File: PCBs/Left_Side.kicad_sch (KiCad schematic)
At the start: 77 parts, among them J1 USB_C_Receptacle, J3 USB_C_Receptacle, U1 W25Q128JVS, U2 XC6206-3.3_SOT, U3 USBLC6-2SC6, U4 RP2040, Y1 Crystal_GND24

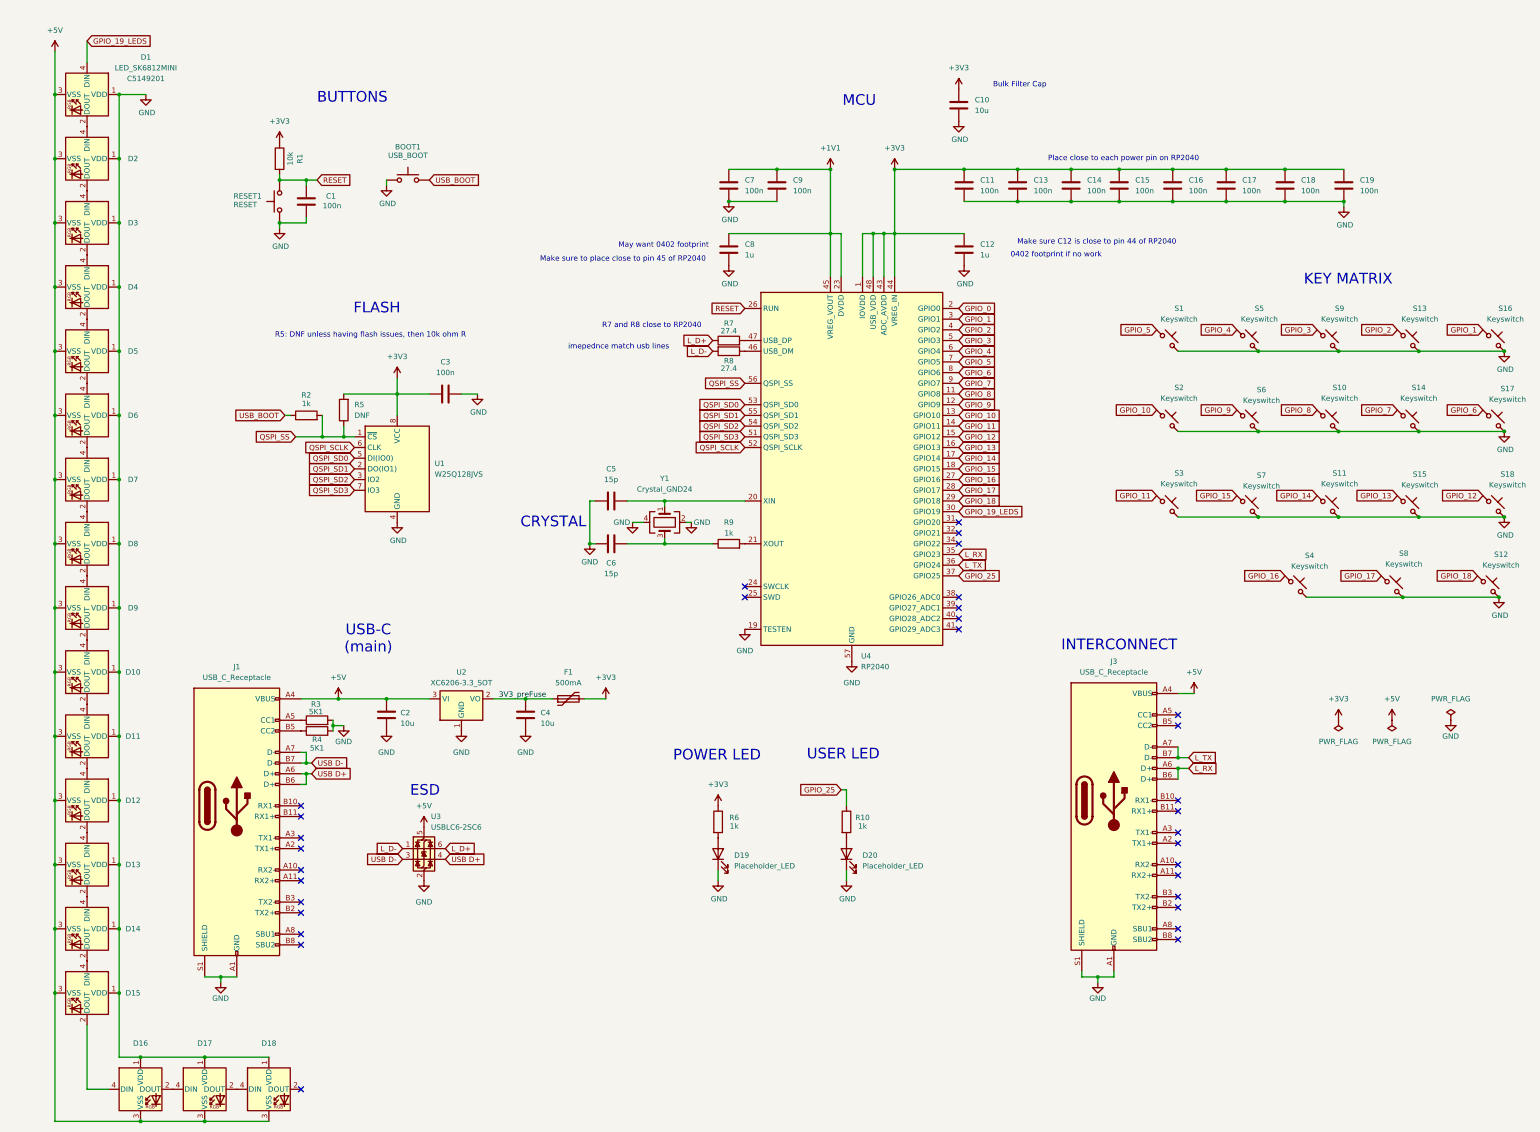
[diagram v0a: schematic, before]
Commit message: added library and routing changes
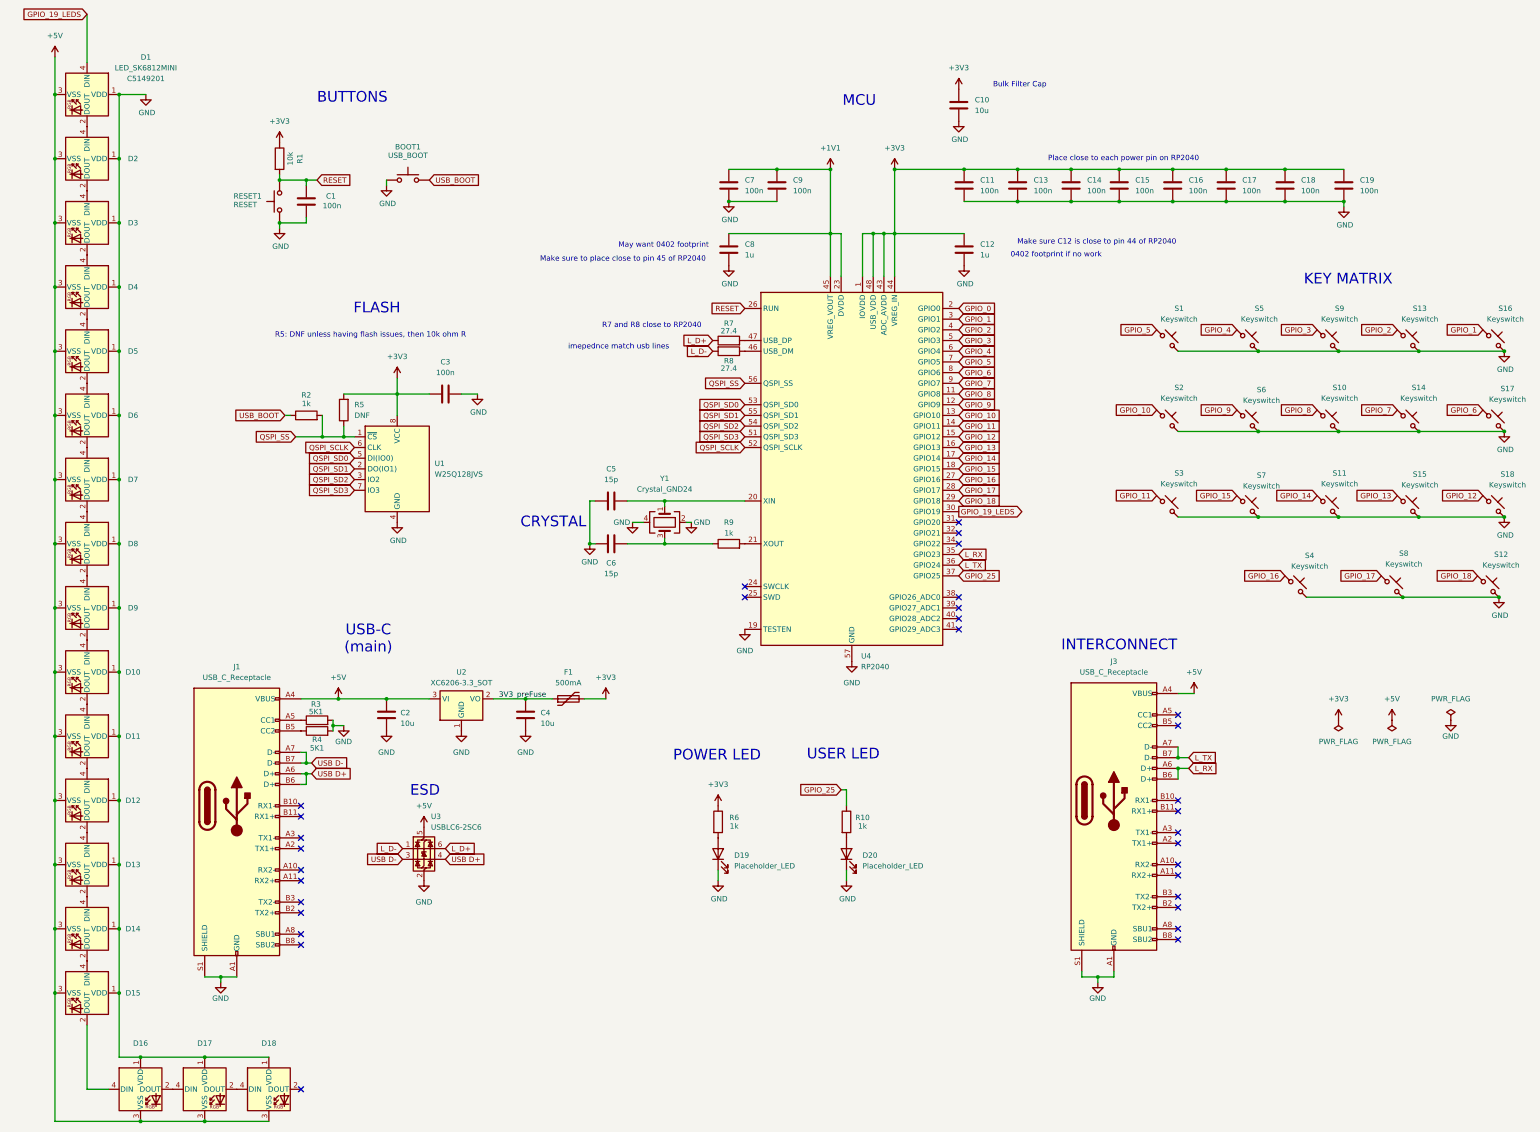
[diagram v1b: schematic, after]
